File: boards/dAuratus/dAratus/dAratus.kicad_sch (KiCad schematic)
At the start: 12 parts, among them SW1 SW_SPDT, U1 ADP7104ARDZ, U2 AVR128DB28-SOIC

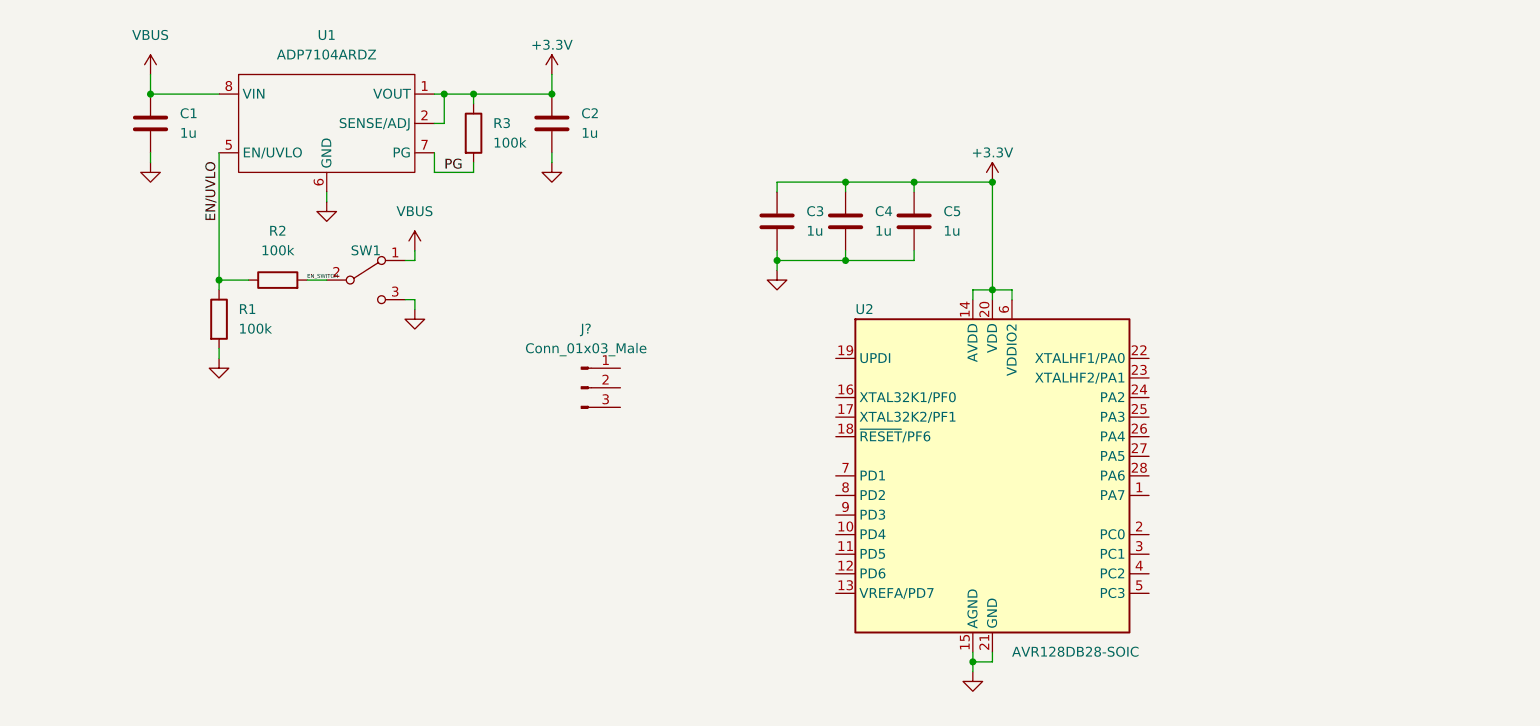
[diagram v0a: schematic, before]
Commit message: Version 1.0 of fan control software.
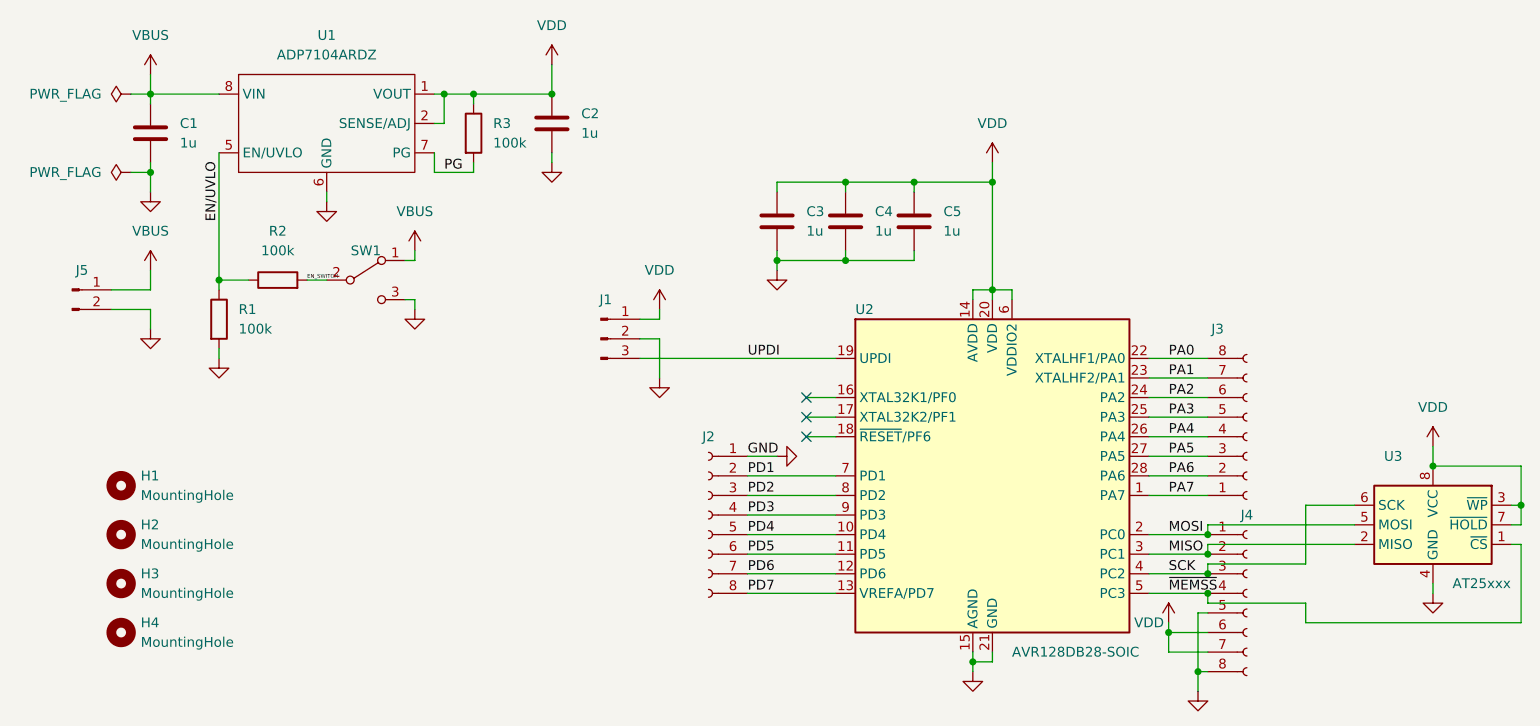
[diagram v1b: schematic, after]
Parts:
- added H1, H2, H3, H4: MountingHole, MountingHole:MountingHole_3.2mm_M3, symbol Mechanical:MountingHole
- added J2, J3, J4: Conn_01x08_Female, Connector_PinHeader_2.54mm:PinHeader_1x08_P2.54mm_Vertical, symbol Connector:Conn_01x08_Female
- added J5: Conn_01x02_Male, Connector_PinHeader_2.54mm:PinHeader_1x02_P2.54mm_Vertical, symbol Connector:Conn_01x02_Male
- added U3: AT25xxx, Package_SO:SOIC-8_3.9x4.9mm_P1.27mm, symbol Memory_EEPROM:AT25xxx
- J1: renamed from J?; footprint (none) -> Connector_PinHeader_2.54mm:PinHeader_1x03_P2.54mm_Vertical
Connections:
- net +3.3V is gone; now on net VDD: C2.1, C3.1, C4.1, C5.1, R3.1, U1.1 (VOUT), U1.2 (SENSE/ADJ), U2.14 (AVDD), U2.20 (VDD), U2.6 (VDDIO2)
- net GND: now also J1.2 (Pin_2), J2.1 (Pin_1), J4.5 (Pin_5), J4.8 (Pin_8), J5.2 (Pin_2), U3.4 (GND)
- net VBUS: now also J5.1 (Pin_1)
- net PA7: now reaches U2.1 (PA7)
- net PA7: now also J3.1 (Pin_1)
- net PD4: now reaches U2.10 (PD4)
- net PD4: now also J2.5 (Pin_5)
- net PD5: now reaches U2.11 (PD5)
- net PD5: now also J2.6 (Pin_6)
- net PD6: now reaches U2.12 (PD6)
- net PD6: now also J2.7 (Pin_7)
- net PD7: now reaches U2.13 (VREFA/PD7)
- net PD7: now also J2.8 (Pin_8)
- net UPDI: now reaches U2.19 (UPDI)
- net UPDI: now also J1.3 (Pin_3)
- net MOSI: now reaches U2.2 (PC0)
- net MOSI: now also J4.1 (Pin_1), U3.5 (MOSI)
- net PA0: now reaches U2.22 (XTALHF1/PA0)
- net PA0: now also J3.8 (Pin_8)
- net PA1: now reaches U2.23 (XTALHF2/PA1)
- net PA1: now also J3.7 (Pin_7)
- net PA2: now reaches U2.24 (PA2)
- net PA2: now also J3.6 (Pin_6)
- net PA3: now reaches U2.25 (PA3)
- net PA3: now also J3.5 (Pin_5)
- net PA4: now reaches U2.26 (PA4)
- net PA4: now also J3.4 (Pin_4)
- net PA5: now reaches U2.27 (PA5)
- net PA5: now also J3.3 (Pin_3)
- net PA6: now reaches U2.28 (PA6)
- net PA6: now also J3.2 (Pin_2)
- net MISO: now reaches U2.3 (PC1)
- net MISO: now also J4.2 (Pin_2), U3.2 (MISO)
- net SCK: now reaches U2.4 (PC2)
- net SCK: now also J4.3 (Pin_3), U3.6 (SCK)
- net ~{MEMSS}: now reaches U2.5 (PC3)
- net ~{MEMSS}: now also J4.4 (Pin_4), U3.1 (~{CS})
- net PD1: now reaches U2.7 (PD1)
- net PD1: now also J2.2 (Pin_2)
- net PD2: now reaches U2.8 (PD2)
- net PD2: now also J2.3 (Pin_3)
- net PD3: now reaches U2.9 (PD3)
- net PD3: now also J2.4 (Pin_4)
- net VDD: now reaches J1.1 (Pin_1)
- net VDD: now also J4.6 (Pin_6), J4.7 (Pin_7), U3.3 (~{WP}), U3.7 (~{HOLD}), U3.8 (VCC)
- no-connect marks 0 -> 3
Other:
- moved on the sheet: C1, J1
